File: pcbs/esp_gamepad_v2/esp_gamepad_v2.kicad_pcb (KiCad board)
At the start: 2 copper layers, 188.5 x 88.9 mm, 70 parts, among them P1 USB_C_Plug_USB2.0, Q1 SI2300, SW1 SW_Push, SW10 SW_Push, SW11 DIP, SW12 SW_Push, SW13 SW_Push, SW14 SW_Push, SW2 SW_Push, SW3 SW_Push, SW4 SW_Push, SW5 SW_Push, SW6 SW_Push, SW7 SW_Push, SW8 SW_Push, SW9 SW_Push, U3 COM-09032, U5 LC709203FQH-02TWG, U6 COM-09032, U7 IP5306

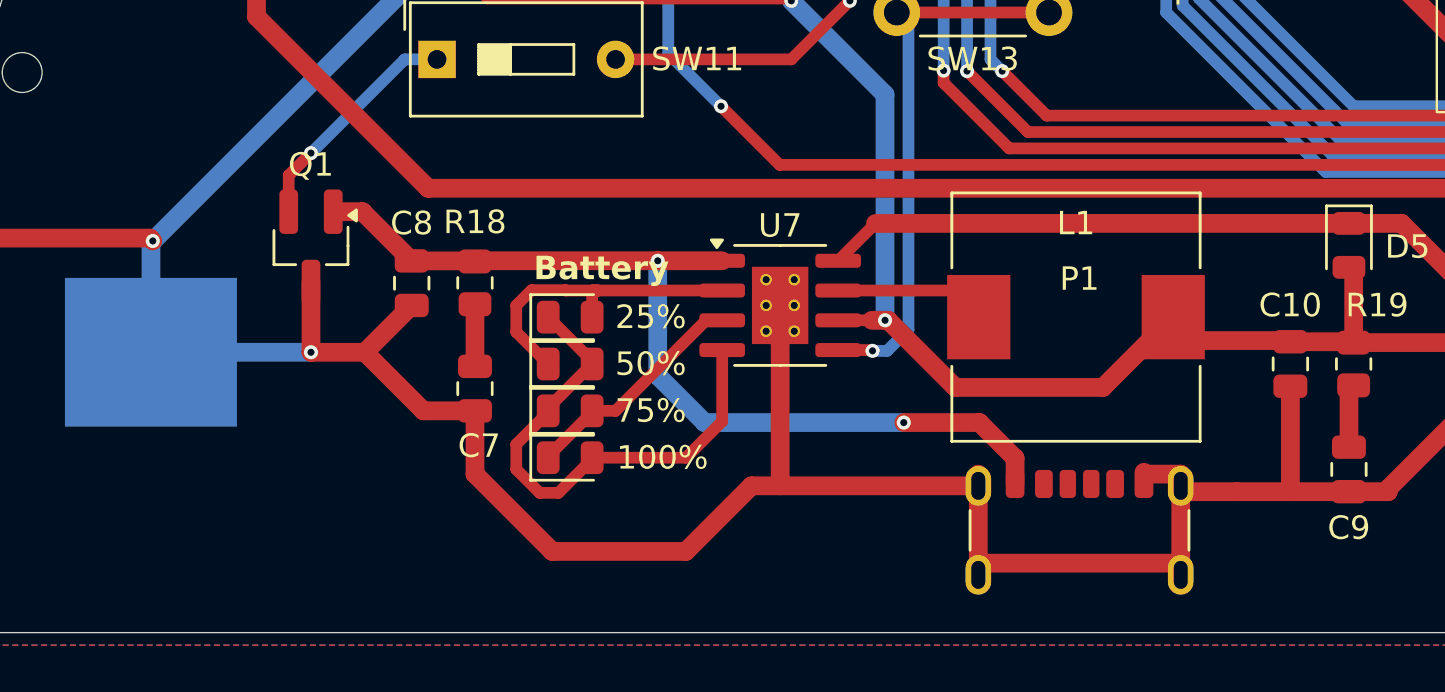
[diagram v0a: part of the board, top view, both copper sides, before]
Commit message: pcb foorprint bug fixing
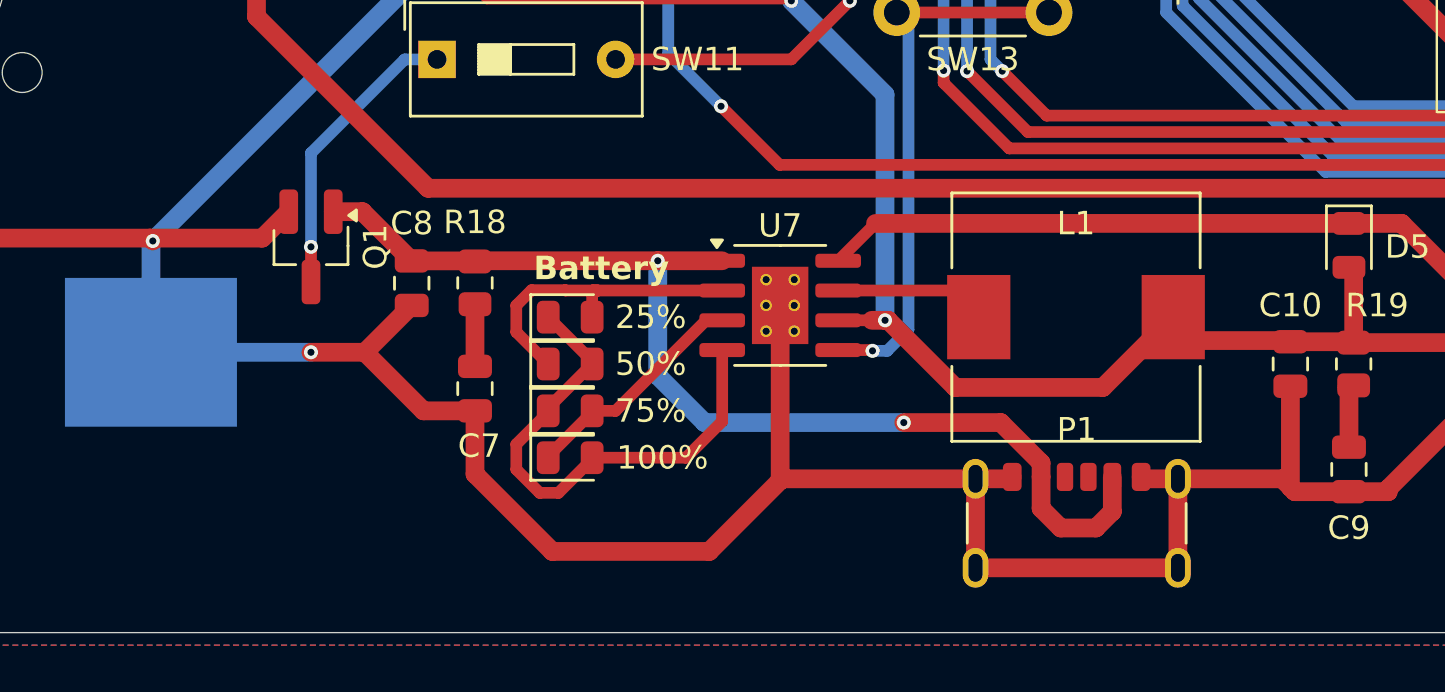
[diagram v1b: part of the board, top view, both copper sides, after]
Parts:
- P1: footprint USB_Type_C:USB_Type_C_6P -> Connector_USB:USB_C_Receptacle_GCT_USB4125-xx-x-0190_6P_TopMnt_Horizontal
- moved P1 2.78 mm to (151.7, 127.4)
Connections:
- Q1 pad 1: Net-(Q2-D) -> /VBUS
- Q1 pad 2: /VBUS -> GND
- Q1 pad 3: GND -> Net-(Q1-D)
- SW11 pad 1: Net-(Q2-D) -> Net-(Q1-D)
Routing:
- net Net-(Q1-D): track 0.00 -> 12.5 mm, vias 0 -> 1
- net Net-(Q2-D): track 9.93 -> 0.00 mm, vias 1 -> 0
- net /VBUS: track 40.2 -> 47.4 mm
- net GND: track 835.8 -> 840.9 mm
